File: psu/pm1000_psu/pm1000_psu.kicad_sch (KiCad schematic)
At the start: 36 parts

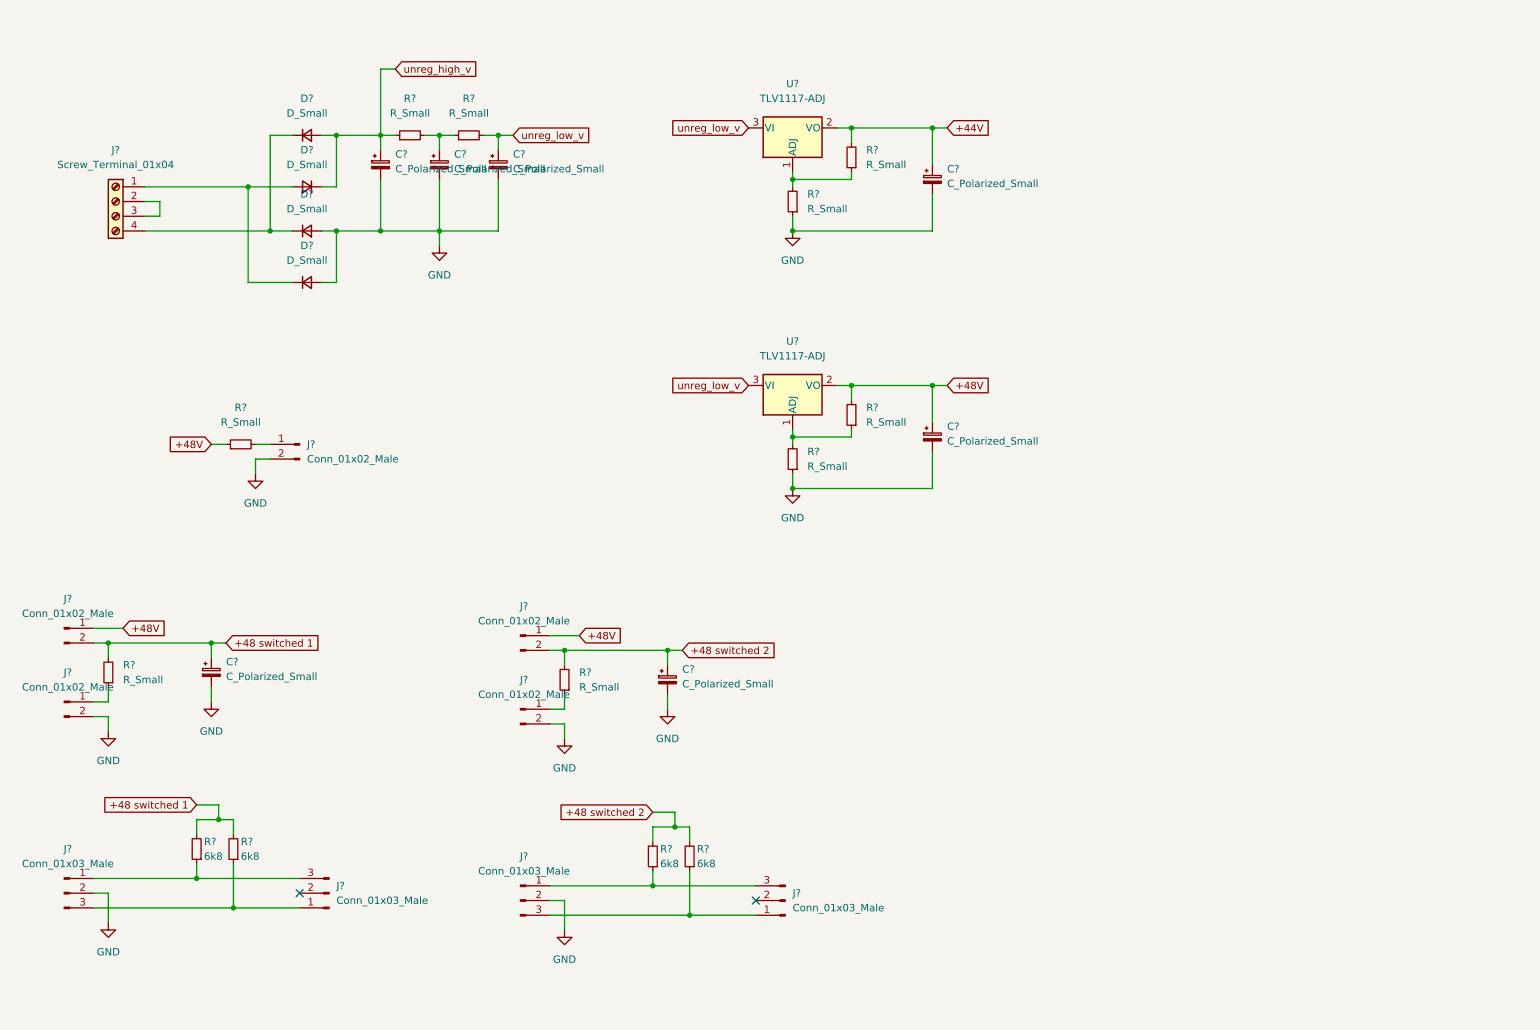
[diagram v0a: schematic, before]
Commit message: clean up schematic
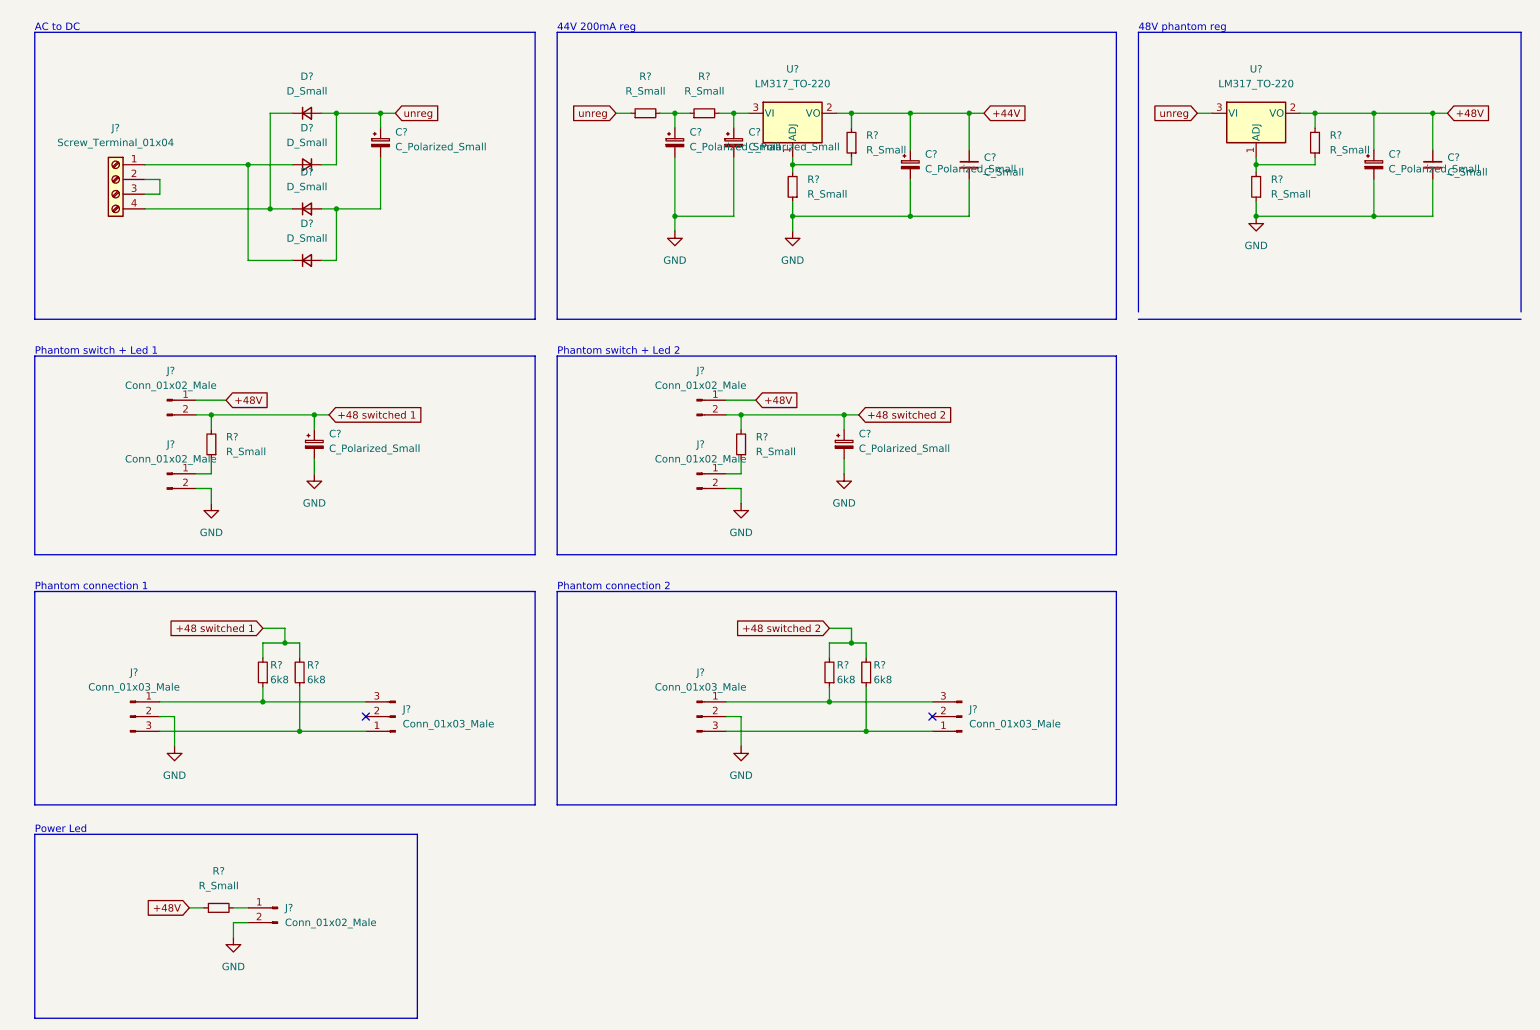
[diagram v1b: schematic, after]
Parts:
- removed C? (x3): C_Polarized_Small, symbol Device:C_Polarized_Small
- removed J?: Conn_01x02_Male, symbol Connector:Conn_01x02_Male
- removed R? (x3): R_Small, symbol Device:R_Small
- removed U? (x2): TLV1117-ADJ, symbol Regulator_Linear:TLV1117-ADJ
- added C? (x2): C_Small, symbol Device:C_Small
- added C? (x3): C_Polarized_Small, symbol Device:C_Polarized_Small
- added J?: Conn_01x02_Male, symbol Connector:Conn_01x02_Male
- added R? (x3): R_Small, symbol Device:R_Small
- added U? (x2): LM317_TO-220, Package_TO_SOT_THT:TO-220-3_Vertical, symbol Regulator_Linear:LM317_TO-220
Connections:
- net +44V: now also C?.1, U?.2 (VO)
- net +48V: now also C?.1, C?.1, R?.1, U?.2 (VO)
- net GND: now also C?.2, C?.2, C?.2, C?.2, C?.2, J?.2 (Pin_2); no longer C?.2, D?.2 (A), D?.2 (A)
- net at R?.1, R?.2: now also U?.1 (ADJ) (x2)
- net unreg_high_v renamed unreg
- net unreg: now also R?.1, U?.3 (VI)
- new net: C?.2, D?.2 (A), D?.2 (A)
- new net: C?.1, R?.1, R?.2
- new net: C?.1, R?.2, U?.3 (VI)
- new net: J?.1 (Pin_1), R?.2
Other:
- note added: "44V 200mA reg"
- note added: "48V phantom reg"
- note added: "AC to DC"
- note added: "Phantom connection 1"
- note added: "Phantom connection 2"
- note added: "Phantom switch + Led 1"
- note added: "Phantom switch + Led 2"
- note added: "Power Led"
- moved on the sheet: C?, D?, J?, R?

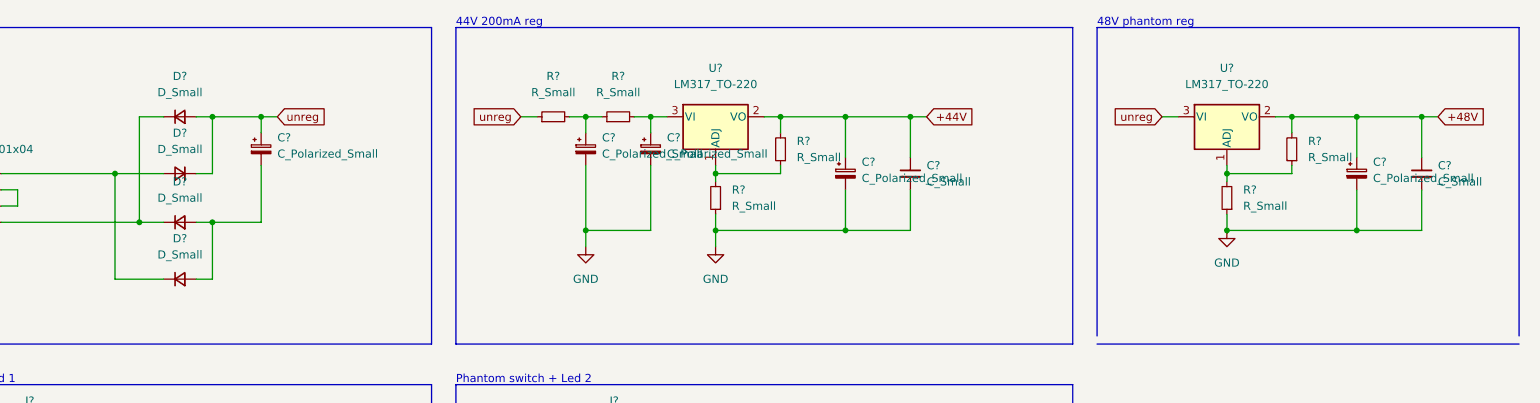
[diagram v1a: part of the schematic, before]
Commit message: update schematic
- add diode footprints
- add reg protection diodes
- add trimmers
- cleanup
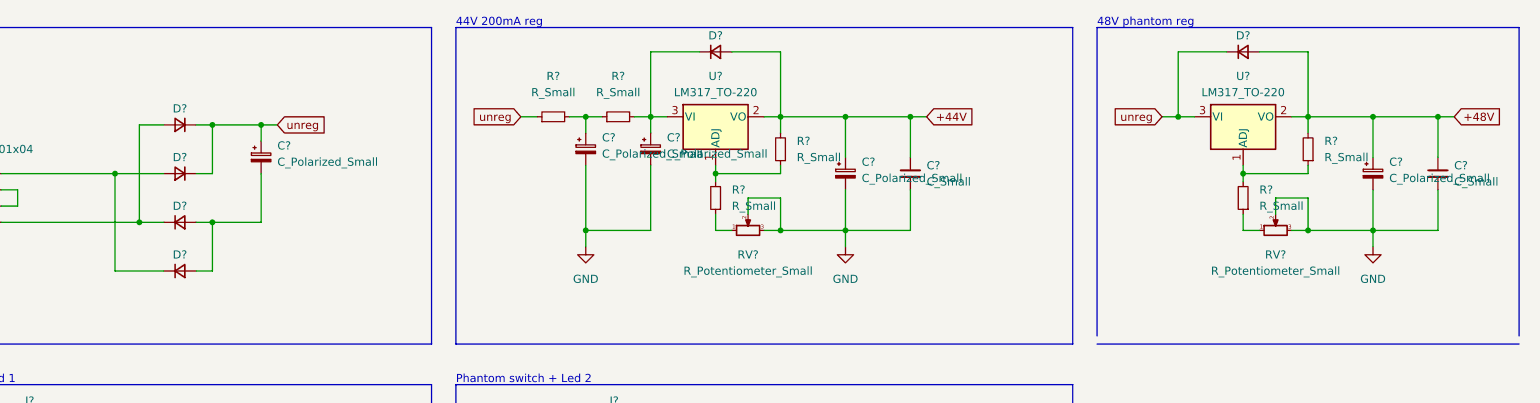
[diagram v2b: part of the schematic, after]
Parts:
- removed D? (x4): D_Small, symbol Device:D_Small
- added D? (x6): 1n4004, Diode_THT:D_DO-41_SOD81_P10.16mm_Horizontal, symbol Device:D_Small
- added RV? (x2): R_Potentiometer_Small, symbol Device:R_Potentiometer_Small
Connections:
- net +44V: now also D?.2 (A)
- net +48V: now also D?.2 (A)
- net GND: now also RV?.2, RV?.2, RV?.3, RV?.3; no longer R?.1, R?.1
- net unreg: now also D?.1 (K), D?.1 (K), D?.1 (K)
- net at J?.1 (Pin_1): now also D?.1 (K), D?.2 (A)
- net at C?.2: now also D?.2 (A), D?.2 (A)
- net at J?.4 (Pin_4): now also D?.1 (K), D?.2 (A)
- net at C?.1, R?.2, U?.3 (VI): now also D?.1 (K)
- new net: R?.1, RV?.1 (x2)
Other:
- moved on the sheet: C?, R?, U?

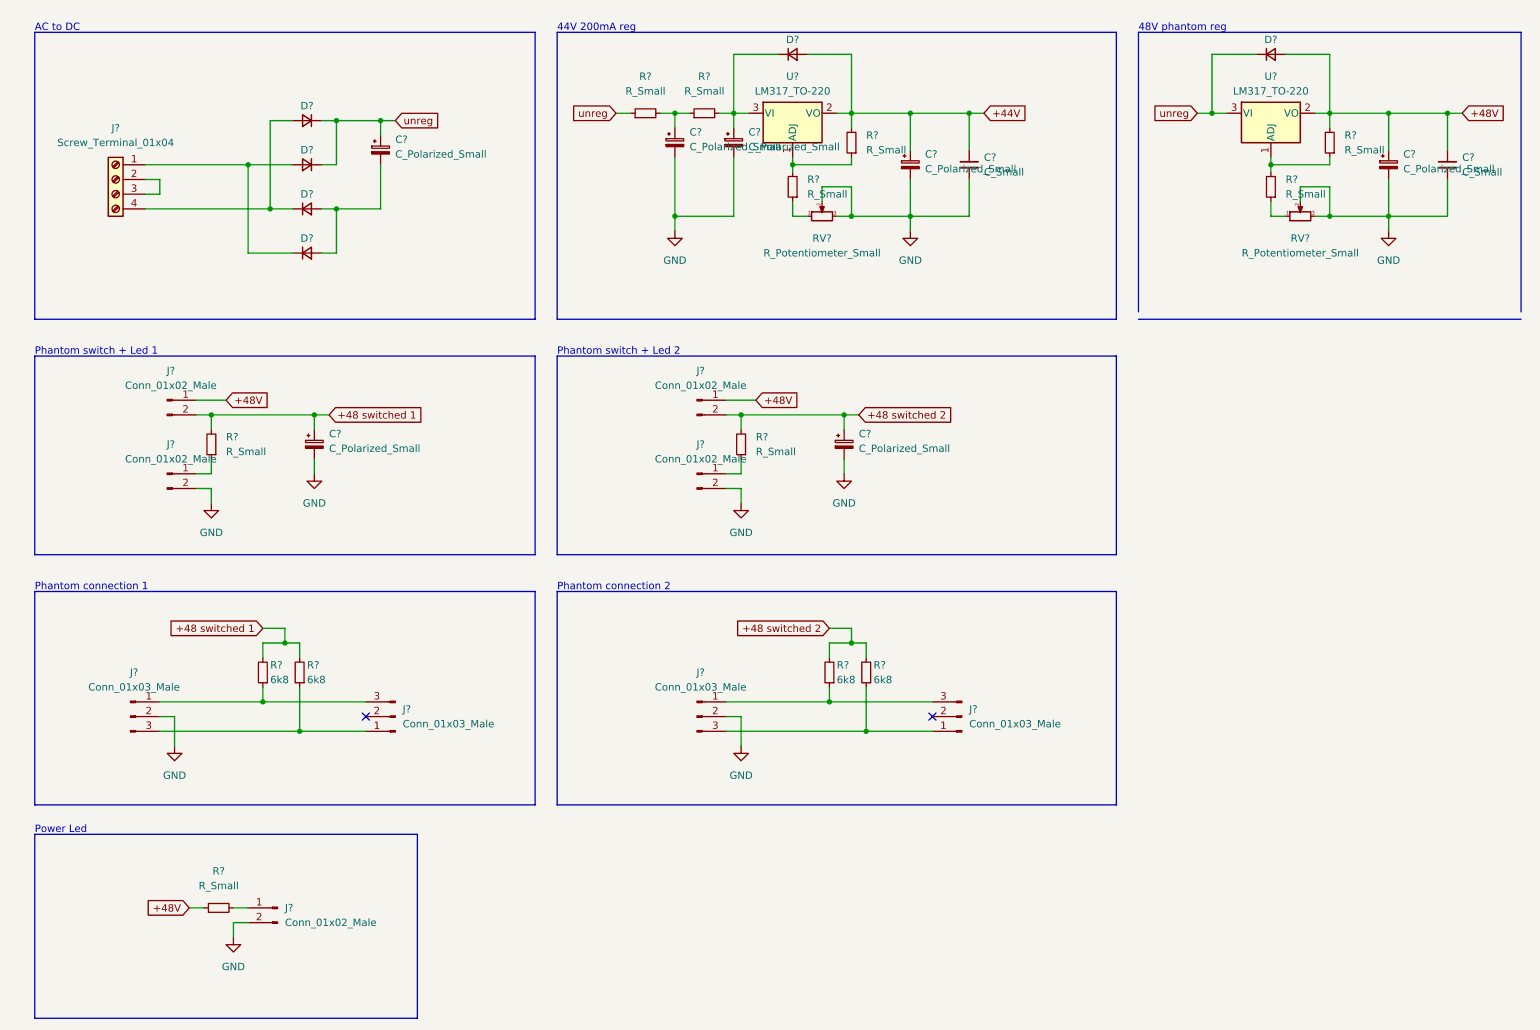
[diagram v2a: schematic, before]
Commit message: calculate values and add some footprints
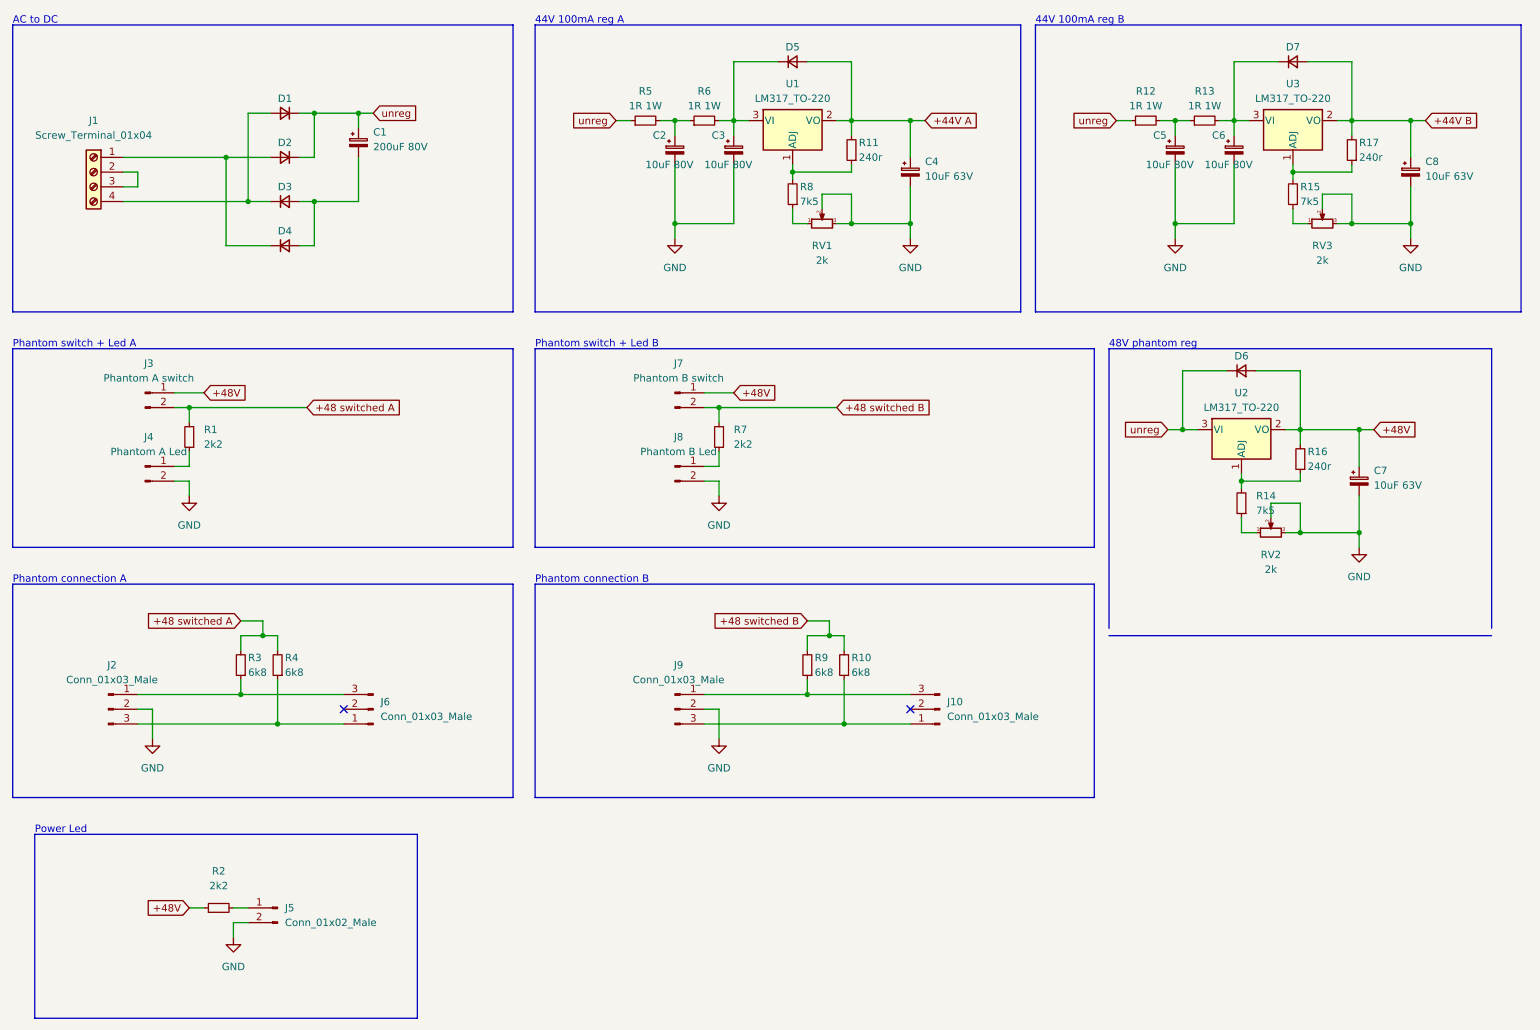
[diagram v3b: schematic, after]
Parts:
- removed C? (x2): C_Small, symbol Device:C_Small
- removed C? (x2): C_Polarized_Small, symbol Device:C_Polarized_Small
- added C5, C6: 10uF 80V, Capacitor_THT:CP_Radial_D6.3mm_P2.50mm, symbol Device:C_Polarized_Small
- added C8: 10uF 63V, Capacitor_THT:CP_Radial_D6.3mm_P2.50mm, symbol Device:C_Polarized_Small
- added D7: 1n4004, Diode_THT:D_DO-41_SOD81_P10.16mm_Horizontal, symbol Device:D_Small
- added R12, R13: 1R 1W, Resistor_THT:R_Axial_DIN0207_L6.3mm_D2.5mm_P10.16mm_Horizontal, symbol Device:R_Small
- added R15: 7k5, Resistor_THT:R_Axial_DIN0207_L6.3mm_D2.5mm_P10.16mm_Horizontal, symbol Device:R_Small
- added R17: 240r, Resistor_THT:R_Axial_DIN0207_L6.3mm_D2.5mm_P10.16mm_Horizontal, symbol Device:R_Small
- added RV3: 2k, Potentiometer_THT:Potentiometer_Bourns_3386F_Vertical, symbol Device:R_Potentiometer_Small
- added U3: LM317_TO-220, Package_TO_SOT_THT:TO-220-3_Vertical, symbol Regulator_Linear:LM317_TO-220
- C1: renamed from C?; value C_Polarized_Small -> 200uF 80V; footprint (none) -> Capacitor_THT:CP_Radial_D12.5mm_P5.00mm
- C2, C3: renamed from C?; value C_Polarized_Small -> 10uF 80V; footprint (none) -> Capacitor_THT:CP_Radial_D6.3mm_P2.50mm
- C4, C7: renamed from C?; value C_Polarized_Small -> 10uF 63V; footprint (none) -> Capacitor_THT:CP_Radial_D6.3mm_P2.50mm
- J3: renamed from J?; value Conn_01x02_Male -> Phantom A switch
- J4: renamed from J?; value Conn_01x02_Male -> Phantom A Led
- J7: renamed from J?; value Conn_01x02_Male -> Phantom B switch
- J8: renamed from J?; value Conn_01x02_Male -> Phantom B Led
- R1, R2, R7: renamed from R?; value R_Small -> 2k2; footprint (none) -> Resistor_THT:R_Axial_DIN0207_L6.3mm_D2.5mm_P10.16mm_Horizontal
- R10, R3, R4, R9: renamed from R?; footprint (none) -> Resistor_THT:R_Axial_DIN0207_L6.3mm_D2.5mm_P10.16mm_Horizontal
- R11, R16: renamed from R?; value R_Small -> 240r; footprint (none) -> Resistor_THT:R_Axial_DIN0207_L6.3mm_D2.5mm_P10.16mm_Horizontal
- R14, R8: renamed from R?; value R_Small -> 7k5; footprint (none) -> Resistor_THT:R_Axial_DIN0207_L6.3mm_D2.5mm_P10.16mm_Horizontal
- R5, R6: renamed from R?; value R_Small -> 1R 1W; footprint (none) -> Resistor_THT:R_Axial_DIN0207_L6.3mm_D2.5mm_P10.16mm_Horizontal
- RV1, RV2: renamed from RV?; value R_Potentiometer_Small -> 2k; footprint (none) -> Potentiometer_THT:Potentiometer_Bourns_3386F_Vertical
- gave numbers to parts that had none: 14
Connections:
- net GND: now also C5.2, C6.2, C8.2, RV3.2, RV3.3
- net unreg: now also R12.1
- net +44V renamed +44V A
- net +48 switched 1 renamed +48 switched A
- net +48 switched 2 renamed +48 switched B
- new net: R15.2, R17.1, U3.1 (ADJ)
- new net: C6.1, D7.1 (K), R13.2, U3.3 (VI)
- new net: C5.1, R12.2, R13.1
- new net: R15.1, RV3.1
- new net +44V B: C8.1, D7.2 (A), R17.2, U3.2 (VO)
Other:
- note added: "44V 100mA reg A"
- note added: "44V 100mA reg B"
- note added: "Phantom connection A"
- note added: "Phantom connection B"
- note added: "Phantom switch + Led A"
- note added: "Phantom switch + Led B"
- note removed: "44V 200mA reg"
- note removed: "Phantom connection 1"
- note removed: "Phantom connection 2"
- note removed: "Phantom switch + Led 1"
- note removed: "Phantom switch + Led 2"
- moved on the sheet: C1, C2, C3, C4, C7, D1, D2, D3, D4, D5, D6, J1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
